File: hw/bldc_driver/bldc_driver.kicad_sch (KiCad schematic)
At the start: 57 parts, among them J1 430450412, J2 B6B-EH-A(LF)(SN), J3 B4B-EH-A(LF)(SN), J4 1733583, SW1 BTSA-N-P-1, U14 SN65HVD230, U15 STM32L431CCTx, U16 SN74LVC1G125DBV, U17 SN74LVC1G125DBV, U8 TPS54202DDC, Y1 Crystal_GND24

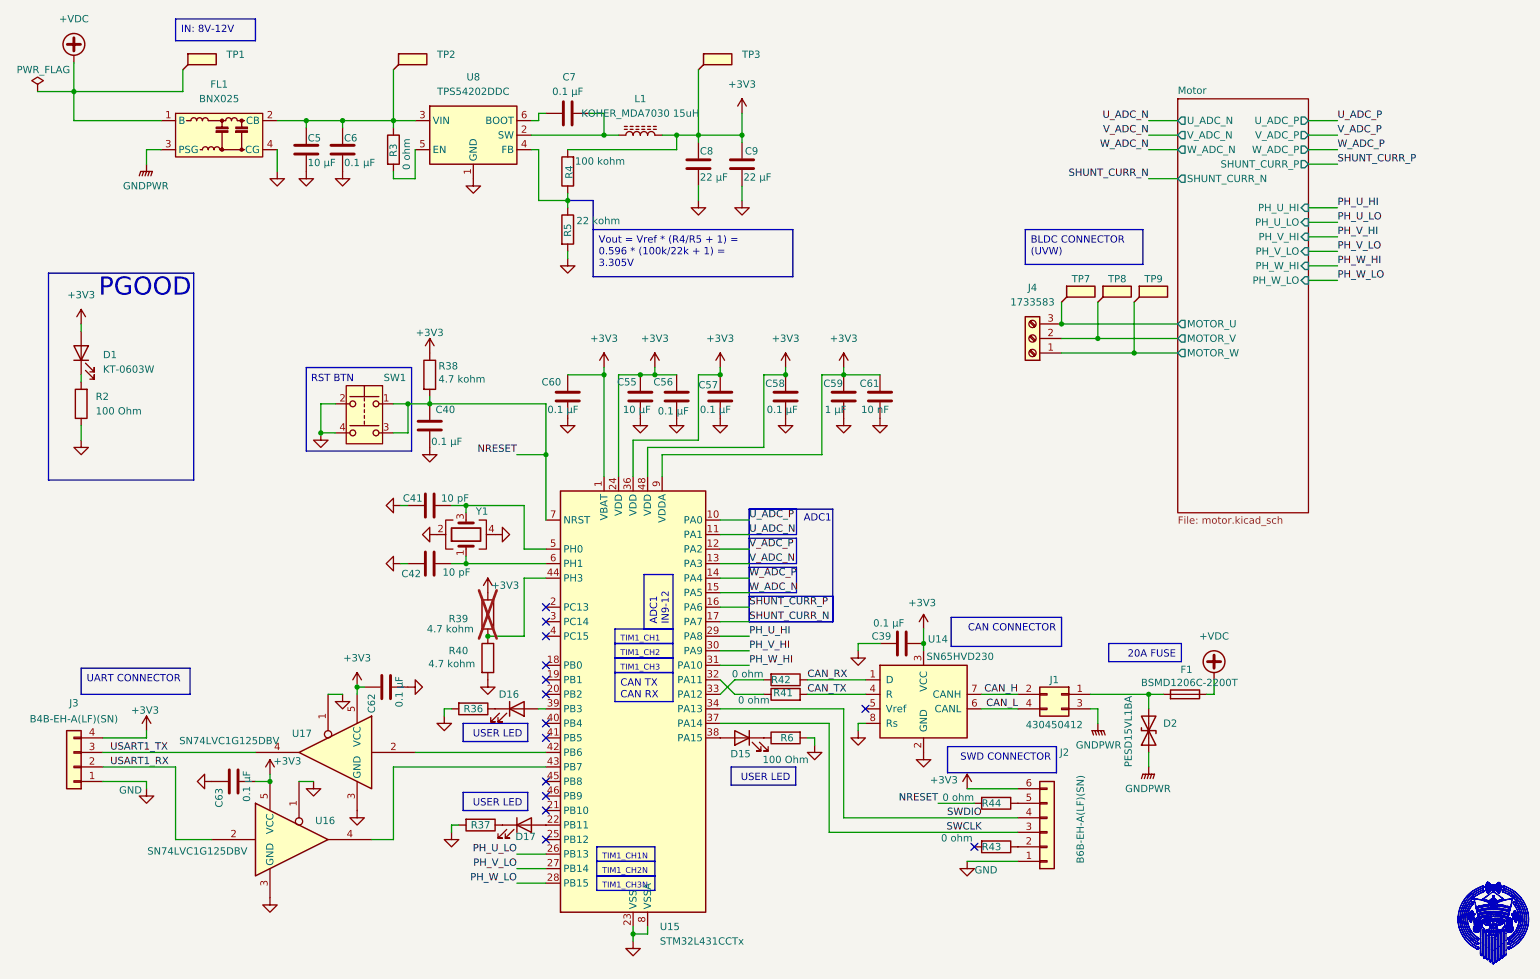
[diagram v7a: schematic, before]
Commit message: fmu: update power supply and other connections
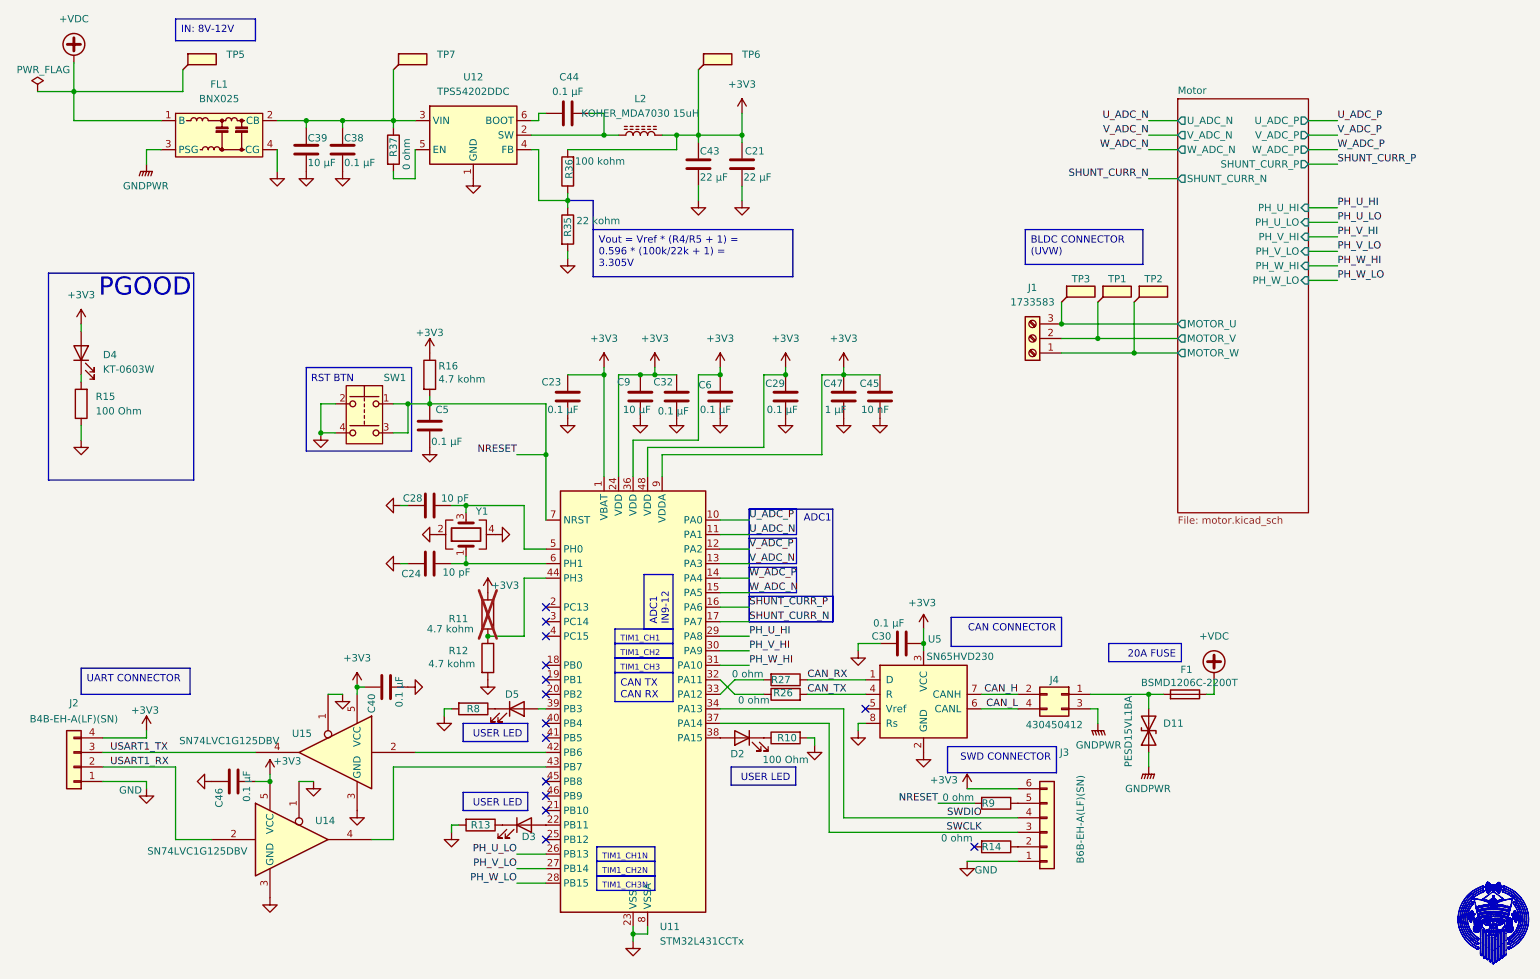
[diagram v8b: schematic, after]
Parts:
- renumbered C9 to C21, C60 to C23, C42 to C24, C41 to C28, C58 to C29, C39 to C30, C56 to C32, C6 to C38, C5 to C39, C62 to C40, C8 to C43, C7 to C44, C61 to C45, C63 to C46, C59 to C47, C40 to C5, C57 to C6, C55 to C9, D2 to D11, D15 to D2, D17 to D3, D1 to D4, D16 to D5, J4 to J1, J3 to J2, J2 to J3, J1 to J4, L1 to L2, R6 to R10, R39 to R11, R40 to R12, R37 to R13, R43 to R14, R2 to R15, R38 to R16, R41 to R26, R42 to R27, R5 to R35, R4 to R36, R3 to R37, R36 to R8, R44 to R9, TP8 to TP1, TP9 to TP2, TP7 to TP3, TP1 to TP5, TP3 to TP6, TP2 to TP7, U15 to U11, U8 to U12, U16 to U14, U17 to U15, U14 to U5
